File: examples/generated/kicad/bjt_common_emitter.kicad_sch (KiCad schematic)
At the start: 6 parts, among them Q1 2N3904

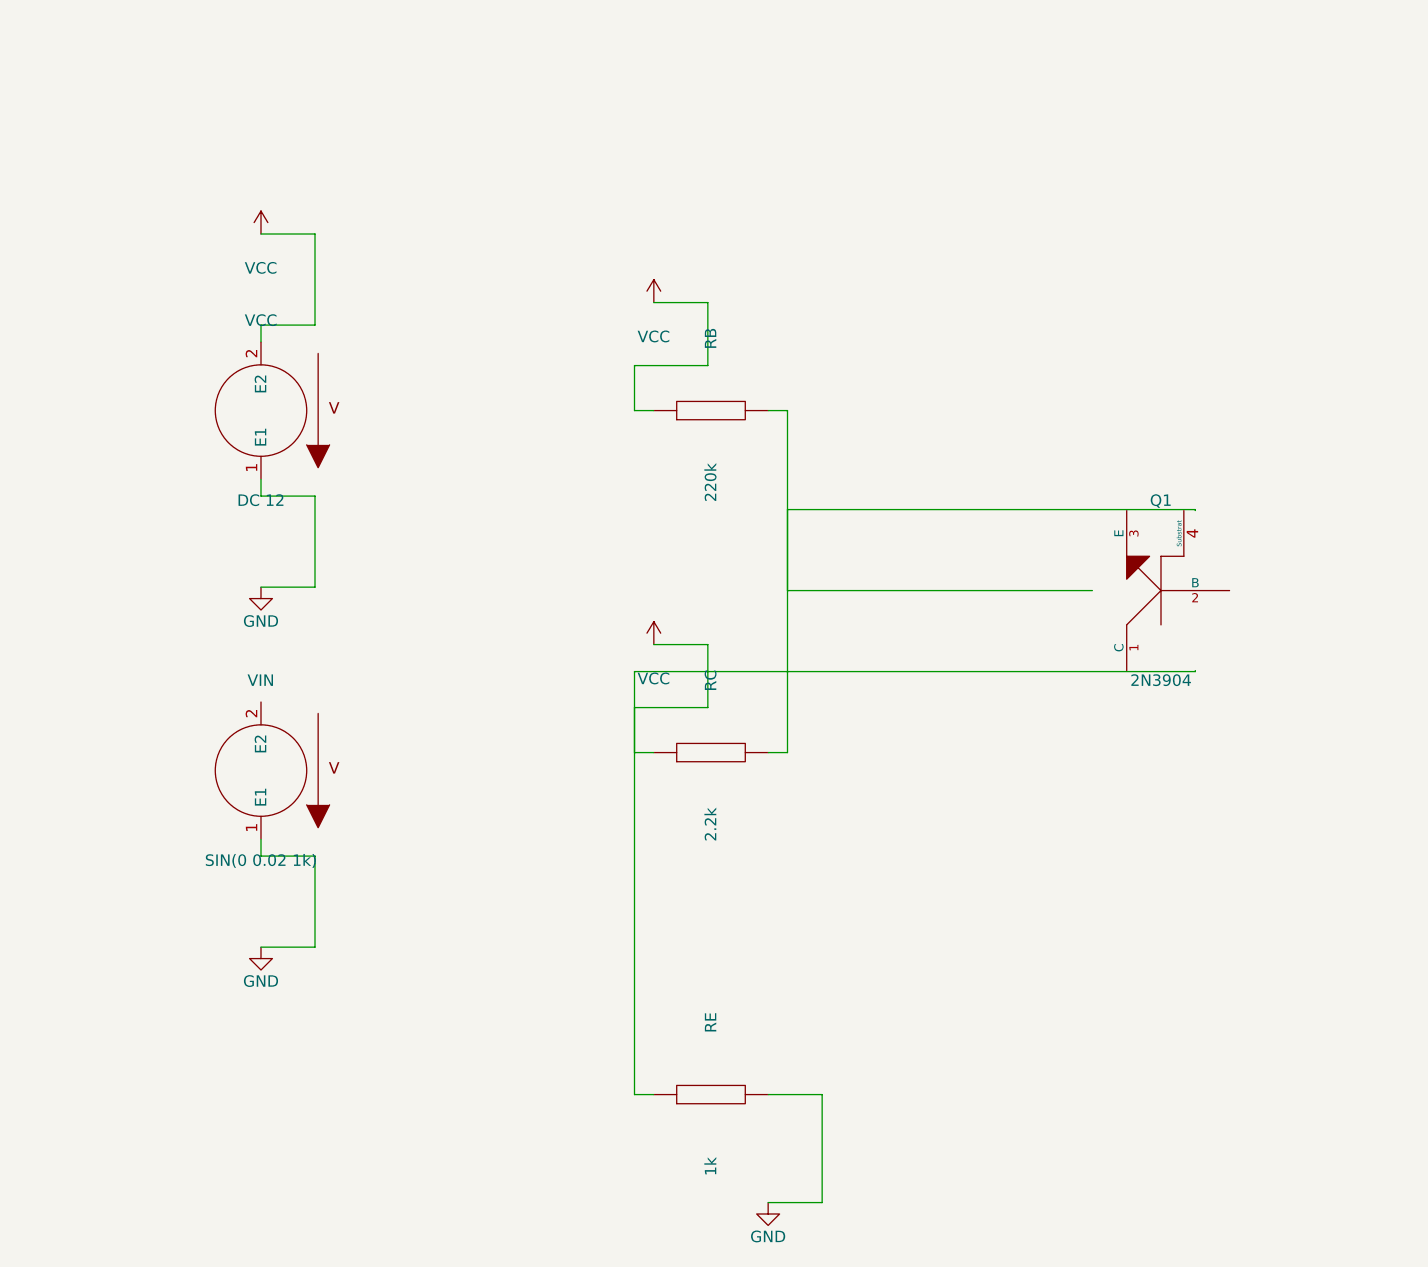
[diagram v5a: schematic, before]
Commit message: Attempt to fix kinking and terminal direction issuses.
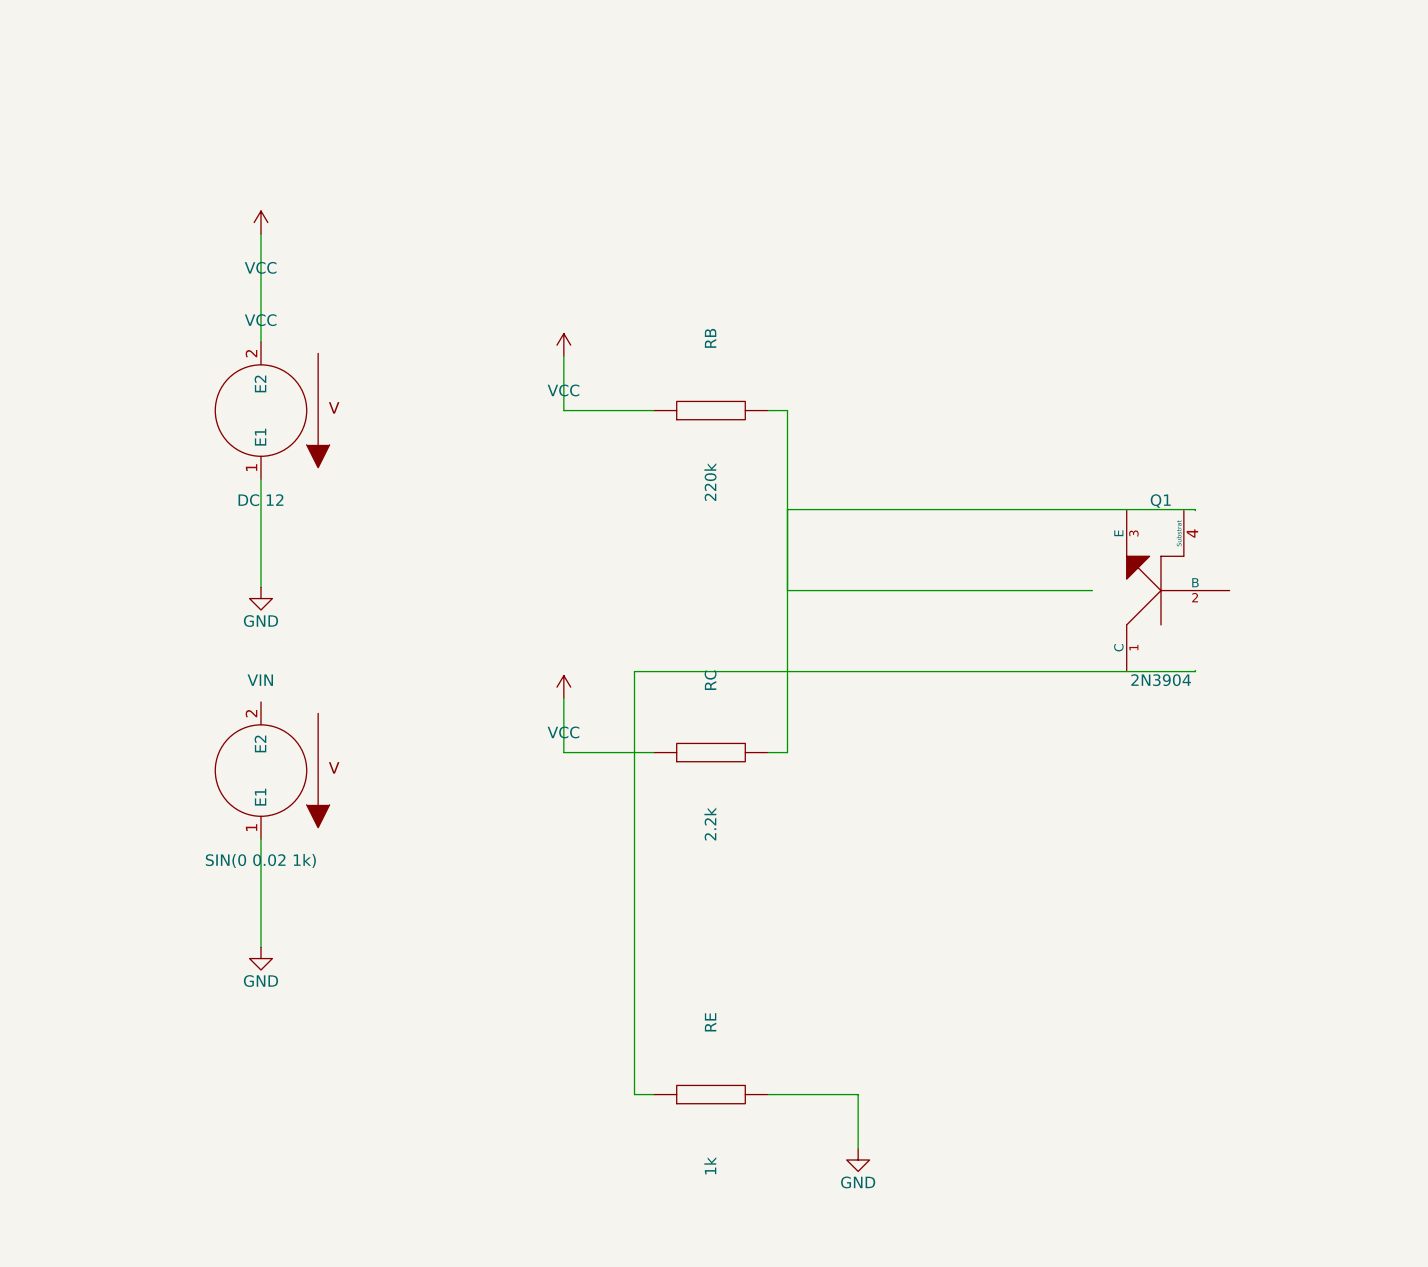
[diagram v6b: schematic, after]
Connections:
- net VCC: no longer RE.1
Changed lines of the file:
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@@
     )
   )
-  (symbol (lib_id "VCC") (at 93.65 58.00 0) (unit 1)
+  (symbol (lib_id "VCC") (at 83.65 64.00 0) (unit 1)
     (in_bom yes) (on_board yes)
-    (property "Reference" "#PWR0004" (at 93.65 54.19 0)
+    (property "Reference" "#PWR0004" (at 83.65 60.19 0)
       (effects (font (size 1.27 1.27)) hide)
     )
-    (property "Value" "VCC" (at 93.65 61.81 0)
+    (property "Value" "VCC" (at 83.65 67.81 0)
       (effects (font (size 1.27 1.27)))
     )
@@
     )
   )
-  (symbol (lib_id "VCC") (at 93.65 96.00 0) (unit 1)
+  (symbol (lib_id "VCC") (at 83.65 102.00 0) (unit 1)
     (in_bom yes) (on_board yes)
-    (property "Reference" "#PWR0005" (at 93.65 92.19 0)
+    (property "Reference" "#PWR0005" (at 83.65 98.19 0)
       (effects (font (size 1.27 1.27)) hide)
     )
-    (property "Value" "VCC" (at 93.65 99.81 0)
+    (property "Value" "VCC" (at 83.65 105.81 0)
       (effects (font (size 1.27 1.27)))
     )
@@
     )
   )
-  (symbol (lib_id "GND") (at 106.35 158.00 0) (unit 1)
+  (symbol (lib_id "GND") (at 116.35 152.00 0) (unit 1)
     (in_bom yes) (on_board yes)
-    (property "Reference" "#PWR0006" (at 106.35 154.19 0)
+    (property "Reference" "#PWR0006" (at 116.35 148.19 0)
       (effects (font (size 1.27 1.27)) hide)
     )
-    (property "Value" "GND" (at 106.35 161.81 0)
+    (property "Value" "GND" (at 116.35 155.81 0)
       (effects (font (size 1.27 1.27)))
     )
@@
     )
   )
-  (wire (pts (xy 50.00 62.38) (xy 50.00 60.50))
+  (wire (pts (xy 50.00 62.38) (xy 50.00 50.38))
     (stroke (width 0) (type solid) (color 0 0 0 0))
   )
-  (wire (pts (xy 50.00 60.50) (xy 56.00 60.50))
+  (wire (pts (xy 50.00 77.62) (xy 50.00 89.62))
     (stroke (width 0) (type solid) (color 0 0 0 0))
   )
-  (wire (pts (xy 56.00 60.50) (xy 56.00 50.38))
+  (wire (pts (xy 50.00 117.62) (xy 50.00 129.62))
     (stroke (width 0) (type solid) (color 0 0 0 0))
   )
-  (wire (pts (xy 56.00 50.38) (xy 50.00 50.38))
+  (wire (pts (xy 93.65 70.00) (xy 83.65 70.00))
     (stroke (width 0) (type solid) (color 0 0 0 0))
   )
-  (wire (pts (xy 50.00 77.62) (xy 50.00 79.50))
+  (wire (pts (xy 83.65 70.00) (xy 83.65 64.00))
     (stroke (width 0) (type solid) (color 0 0 0 0))
   )
-  (wire (pts (xy 50.00 79.50) (xy 56.00 79.50))
+  (wire (pts (xy 93.65 108.00) (xy 83.65 108.00))
     (stroke (width 0) (type solid) (color 0 0 0 0))
   )
-  (wire (pts (xy 56.00 79.50) (xy 56.00 89.62))
+  (wire (pts (xy 83.65 108.00) (xy 83.65 102.00))
     (stroke (width 0) (type solid) (color 0 0 0 0))
   )
-  (wire (pts (xy 56.00 89.62) (xy 50.00 89.62))
+  (wire (pts (xy 106.35 146.00) (xy 116.35 146.00))
     (stroke (width 0) (type solid) (color 0 0 0 0))
   )
-  (wire (pts (xy 50.00 117.62) (xy 50.00 119.50))
+  (wire (pts (xy 116.35 146.00) (xy 116.35 152.00))
     (stroke (width 0) (type solid) (color 0 0 0 0))
   )
-  (wire (pts (xy 50.00 119.50) (xy 56.00 119.50))
-    (stroke (width 0) (type solid) (color 0 0 0 0))
-  )
-  (wire (pts (xy 56.00 119.50) (xy 56.00 129.62))
-    (stroke (width 0) (type solid) (color 0 0 0 0))
-  )
-  (wire (pts (xy 56.00 129.62) (xy 50.00 129.62))
-    (stroke (width 0) (type solid) (color 0 0 0 0))
-  )
-  (wire (pts (xy 93.65 70.00) (xy 91.50 70.00))
-    (stroke (width 0) (type solid) (color 0 0 0 0))
-  )
-  (wire (pts (xy 91.50 70.00) (xy 91.50 65.00))
-    (stroke (width 0) (type solid) (color 0 0 0 0))
-  )
-  (wire (pts (xy 91.50 65.00) (xy 99.65 65.00))
-    (stroke (width 0) (type solid) (color 0 0 0 0))
-  )
-  (wire (pts (xy 99.65 65.00) (xy 99.65 58.00))
-    (stroke (width 0) (type solid) (color 0 0 0 0))
-  )
-  (wire (pts (xy 99.65 58.00) (xy 93.65 58.00))
-    (stroke (width 0) (type solid) (color 0 0 0 0))
-  )
-  (wire (pts (xy 93.65 108.00) (xy 91.50 108.00))
-    (stroke (width 0) (type solid) (color 0 0 0 0))
-  )
-  (wire (pts (xy 91.50 108.00) (xy 91.50 103.00))
-    (stroke (width 0) (type solid) (color 0 0 0 0))
-  )
-  (wire (pts (xy 91.50 103.00) (xy 99.65 103.00))
-    (stroke (width 0) (type solid) (color 0 0 0 0))
-  )
-  (wire (pts (xy 99.65 103.00) (xy 99.65 96.00))
-    (stroke (width 0) (type solid) (color 0 0 0 0))
-  )
-  (wire (pts (xy 99.65 96.00) (xy 93.65 96.00))
-    (stroke (width 0) (type solid) (color 0 0 0 0))
-  )
-  (wire (pts (xy 106.35 146.00) (xy 112.35 146.00))
-    (stroke (width 0) (type solid) (color 0 0 0 0))
-  )
-  (wire (pts (xy 112.35 146.00) (xy 112.35 158.00))
-    (stroke (width 0) (type solid) (color 0 0 0 0))
-  )
-  (wire (pts (xy 112.35 158.00) (xy 106.35 158.00))
-    (stroke (width 0) (type solid) (color 0 0 0 0))
-  )

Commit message: Attempt to fix more terminal issues.
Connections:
- net GND: now also RE.1; no longer RE.2
- net at RB.2, RC.2: now also VCC.2 (E2)
- net at VIN.2 (E2): now also RB.1
- removed net VCC: RB.1, RC.1, VCC.2 (E2)
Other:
- moved on the sheet: Q1, RB, RC, RE, VCC, VIN
